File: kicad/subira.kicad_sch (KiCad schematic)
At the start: 35 parts, among them J1 USB_C_Receptacle_USB2.0_14P, SW1 SW_Push, U1 ESP32-S3-WROOM-1, U2 AMS1117-3.3, U3 BMI270, U4 LSM9DS1

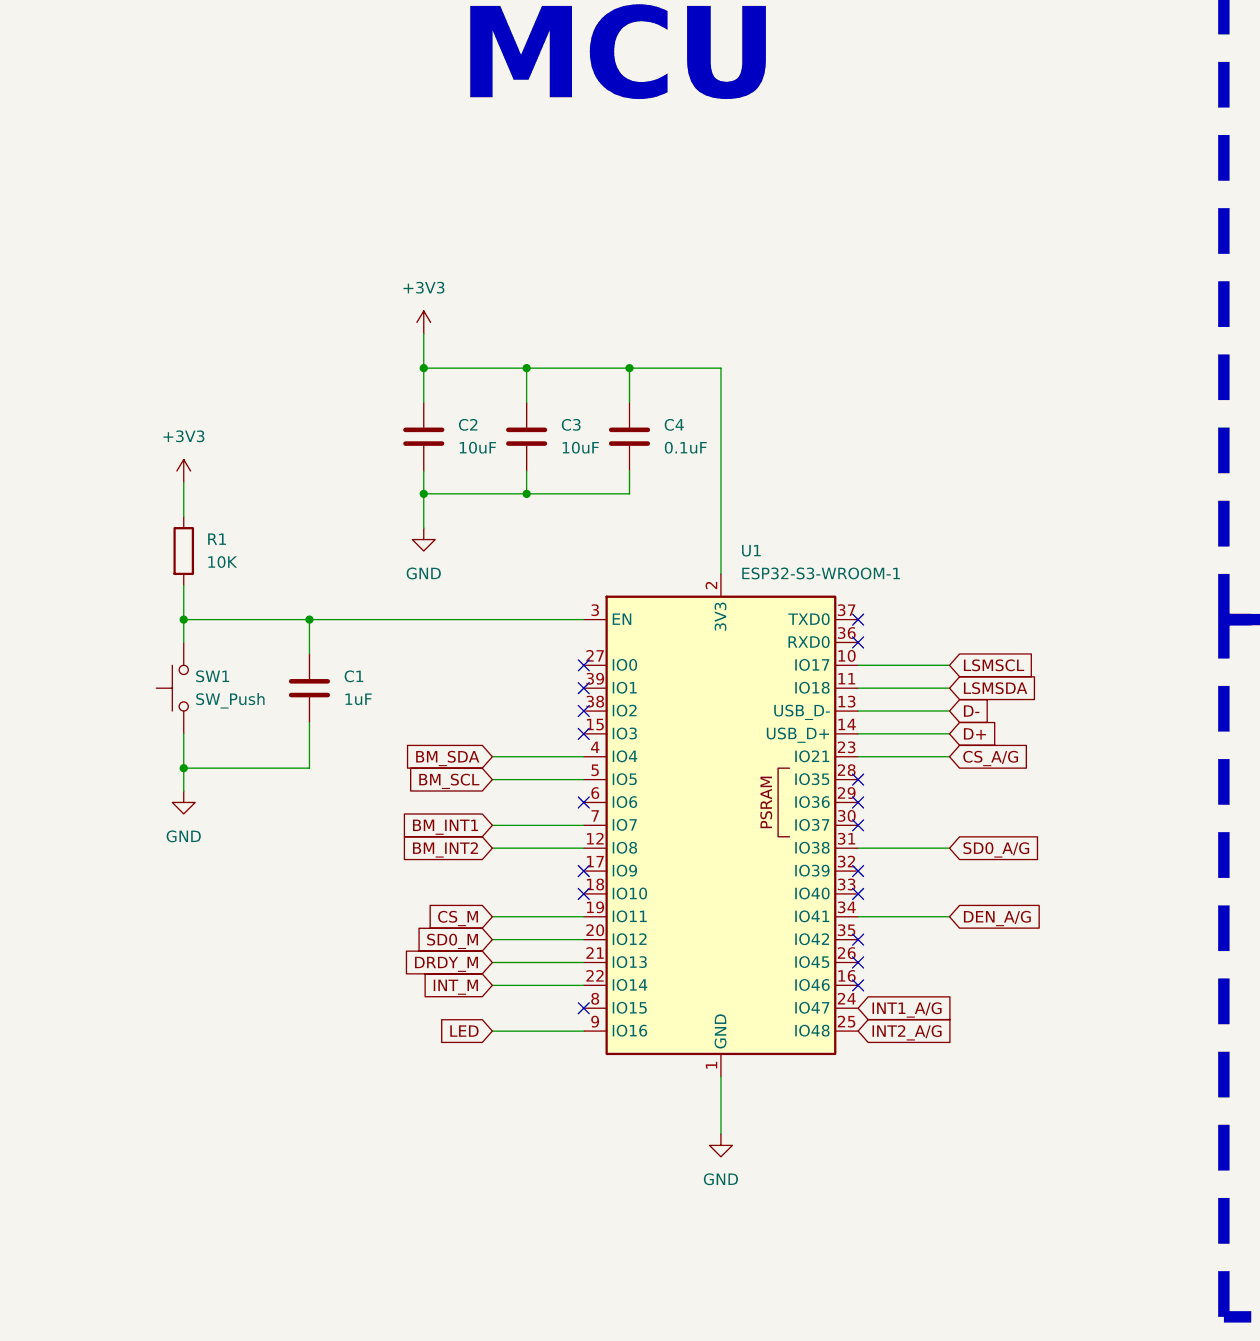
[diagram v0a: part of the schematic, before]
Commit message: fix: enable usb boot option
Fixes https://github.com/rodneyosodo/subira/issues/2
Fixes https://github.com/rodneyosodo/subira/issues/1
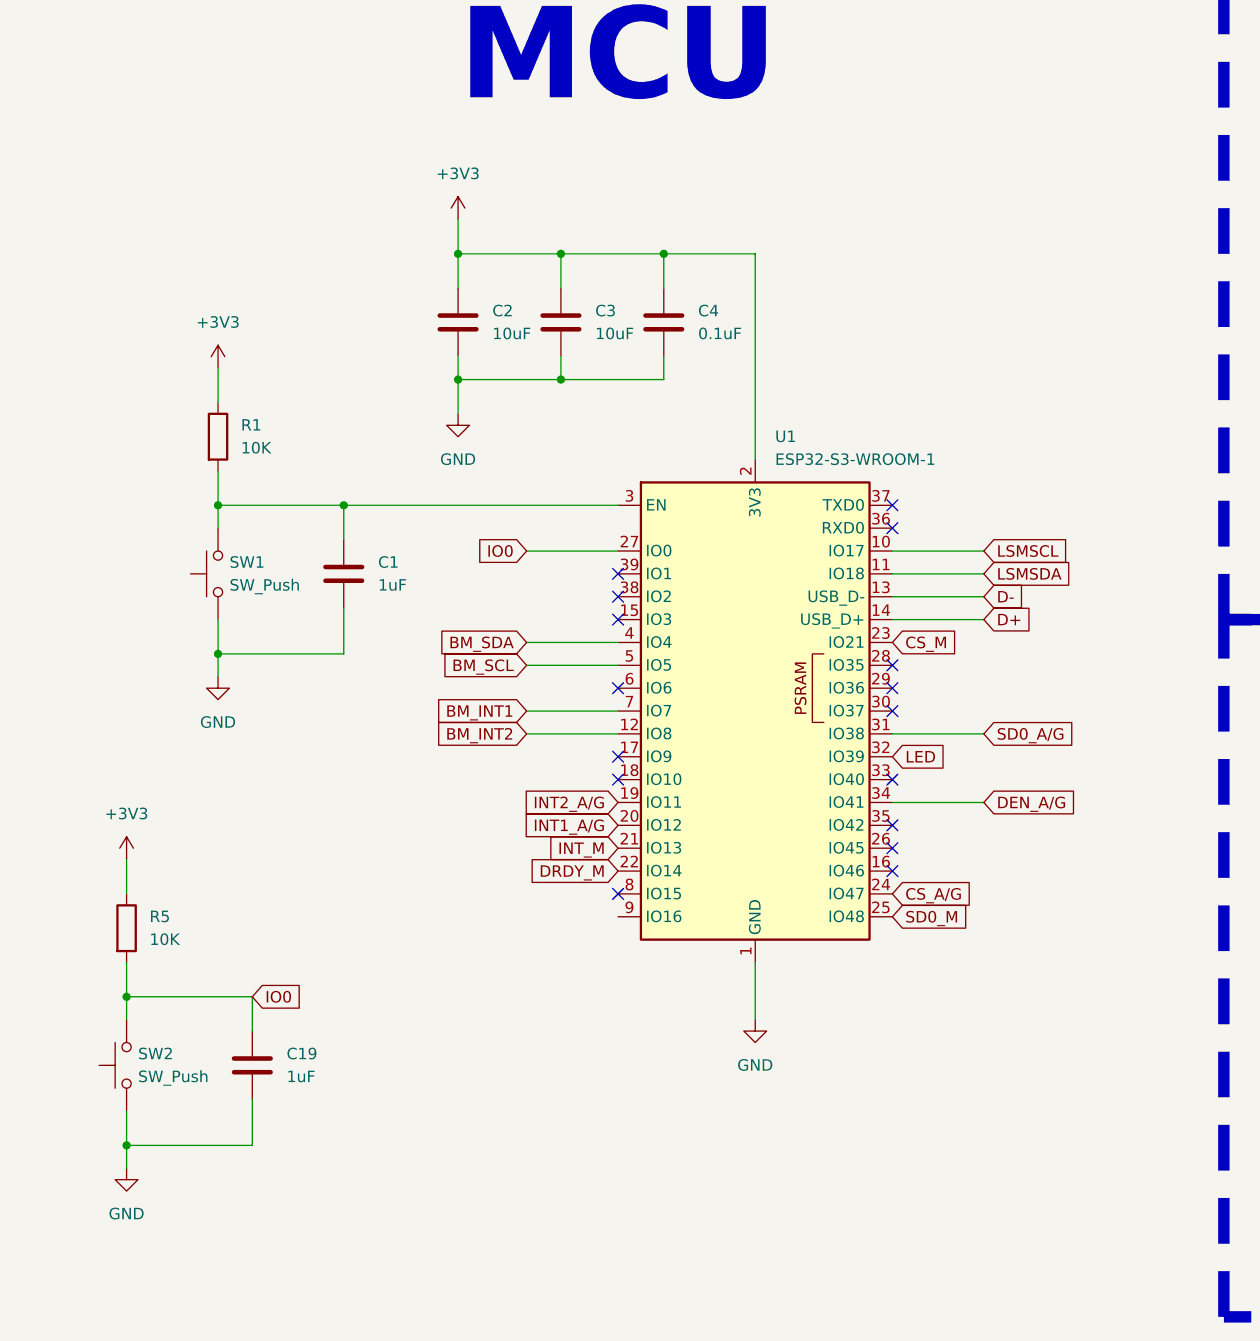
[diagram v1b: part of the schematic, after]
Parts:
- added C19: 1uF, Capacitor_SMD:C_0603_1608Metric_Pad1.08x0.95mm_HandSolder, symbol Device:C
- added R5: 10K, Resistor_SMD:R_0603_1608Metric_Pad0.98x0.95mm_HandSolder, symbol Device:R
- added SW2: SW_Push, Button_Switch_SMD:SW_Push_SPST_NO_Alps_SKRK, symbol Switch:SW_Push
- SW1: footprint Button_Switch_SMD:SW_Push_1P1T_XKB_TS-1187A -> Button_Switch_SMD:SW_Push_SPST_NO_Alps_SKRK; JLCPCB C318884 -> C720477
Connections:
- net +3V3: now also R5.1
- net CS_A/G: now also U1.24 (IO47); no longer U1.23 (IO21)
- net CS_M: now also U1.23 (IO21); no longer U1.19 (IO11)
- net DRDY_M: now also U1.22 (IO14); no longer U1.21 (IO13)
- net GND: now also C19.2, SW2.1
- net INT1_A/G: now also U1.20 (IO12); no longer U1.24 (IO47)
- net INT2_A/G: now also U1.19 (IO11); no longer U1.25 (IO48)
- net INT_M: now also U1.21 (IO13); no longer U1.22 (IO14)
- net LED: now also U1.32 (IO39); no longer U1.9 (IO16)
- net SD0_M: now also U1.25 (IO48); no longer U1.20 (IO12)
- net IO0: now reaches U1.27 (IO0)
- net IO0: now also C19.1, R5.2, SW2.2
- no-connect marks 23 -> 21
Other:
- moved on the sheet: C1, C2, C3, C4, R1, SW1, U1

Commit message: fix(schematic): add 5.1K pull up resistors
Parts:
- added R6, R7, R8, R9: 5.1K, Resistor_SMD:R_0603_1608Metric_Pad0.98x0.95mm_HandSolder, symbol Device:R
- renumbered C19 to C1, C9 to C10, C10 to C11, C11 to C12, C12 to C13, C13 to C14, C14 to C15, C15 to C16, C16 to C17, C17 to C18, C18 to C19, C1 to C2, C2 to C3, C3 to C4, C4 to C5, C5 to C6, C6 to C7, C7 to C8, C8 to C9, R5 to R1, R1 to R2, R2 to R3, R3 to R4, R4 to R5, SW2 to SW1, SW1 to SW2
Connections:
- net +3V3: now also R6.1, R7.1, R8.1, R9.1
- net BM_SCL: now also R9.2
- net BM_SDA: now also R8.2
- net LSMSCL: now also R7.2
- net LSMSDA: now also R6.2
